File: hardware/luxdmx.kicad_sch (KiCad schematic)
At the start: 97 parts, among them J1 XLR-5 NC5FAH, J2 USB-C, J3 HY931147C, J4 DISP SH9, J5 XLR-5 NC5FAH, J6 EXP SH9, J7 DMX-OUT A, J8 DMX-OUT B, SW1 BOOT, SW2 RST, U1 ESP32-S3-WROOM-1-N8R2, U2 W5500, U4 SY8089, U5 ISO3086DWR, U6 ISO3086DWR, U7 DP9900M-5V, U8 USBLC6-2SC6, U9 TPS2116DRLR, Y1 25MHz

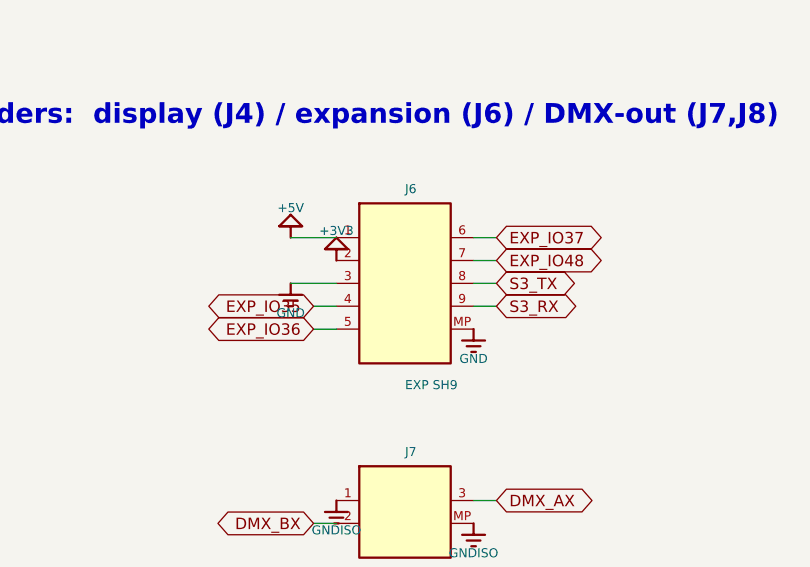
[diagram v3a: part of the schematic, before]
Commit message: hw: v6.0 -- give J4 and J6 the same power pins so a swapped cable stops killing displays
J4 (display) and J6 (expansion) are the same JST SH 9-pin part sitting 9mm apart, so a
cable happily plugs into either one. Their power pins did not agree though:

  J4:  1 = +3V3   2 = GND    3.. = signals
  J6:  1 = +5V    2 = +3V3   3   = GND   4.. = signals

so putting the display on J6 fed it +5V on VCC and +3V3 on GND. That is not a theoretical
hazard, it killed a panel on my bench. The other direction is nasty too: an expansion board
in J4 returns its whole ground current through IO4.

J6 is now 1=+3V3 2=GND 3..8=signals 9=GND, matching J4. Worst case for a mixed-up cable is
now that some 3V3 CMOS signals land in the wrong places, which both sides shrug off. A
display plugged into J6 lands RST on GND and just sits there in reset, dark but fine.

Why J6 and not J4: whichever header moves invalidates its own cables, and re-pinning J4
would have put +5V on every display cable that already exists, so the exact same dead
display with a new cause. J6's pinout only landed in v5.2 and nothing is built against it
yet, so it is the cheap one to change.

Two things fall out of that:

  * +5V is gone from J6. Feed 5V loads from your own supply.
  * pin 9 is a second GND rather than a 7th GPIO, because there is no free non-strapping
    GPIO left on the module (IO3/IO45/IO46 are all strapping pins). An extra return on a
    6-signal 1mm header is the better use anyway, and it is what makes a mis-plugged
    display land RST on ground.

New hard gate, scripts/validate_header_parity.py, wired in as gate 8. It re-checks the
invariant on the board itself every run: fatal if two different rails share a pin position
or a positive rail sits opposite a signal, GND-vs-signal allowed since that is current
limited and no worse than the GPIO-vs-GPIO contention we already accept. Ran it against the
old board first to make sure it actually catches the bug, and it fails on exactly pins 1
and 2.

Re-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
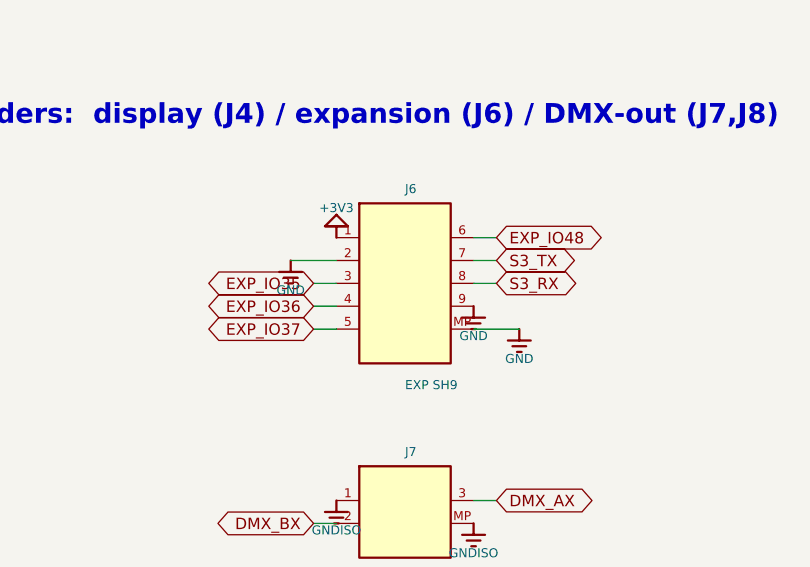
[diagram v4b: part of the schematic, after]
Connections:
- net +3V3: now also J6.1; no longer J6.2
- net +5V: no longer J6.1
- net EXP_IO35: now also J6.3; no longer J6.4
- net EXP_IO36: now also J6.4; no longer J6.5
- net EXP_IO37: now also J6.5; no longer J6.6
- net EXP_IO48: now also J6.6; no longer J6.7
- net GND: now also J6.2, J6.9; no longer J6.3
- net S3_RX: now also J6.8; no longer J6.9
- net S3_TX: now also J6.7; no longer J6.8
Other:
- title: LuxDMX v5.00 - Art-Net/sACN -> isolated DMX gateway -> LuxDMX v6.0 - Art-Net/sACN -> isolated DMX gateway
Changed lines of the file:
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@@
 	(generator_version "9.0")
 	(paper "User" 469.84 529.98)
-	(title_block (title "LuxDMX v5.00 - Art-Net/sACN -> isolated DMX gateway") (rev "v5.00") (comment 1 "auto-generated from luxdmx.net by gen_schematic.py"))
+	(title_block (title "LuxDMX v6.0 - Art-Net/sACN -> isolated DMX gateway") (rev "v6.0") (comment 1 "auto-generated from luxdmx.net by gen_schematic.py"))
 	(text "U1  ESP32-S3-WROOM-1  +  reset / boot" (exclude_from_sim no) (at 12.7 28.4 0) (effects (font (size 2.2 2.2) (bold yes)) (justify left bottom)))
 	(symbol (lib_id "luxdmx:ESP32-S3-WROOM-1-N8R2") (at 132.08 85.09 0) (unit 1) (exclude_from_sim no) (in_bom yes) (on_board yes) (dnp no)
@@
 	(wire (pts (xy 139.7 414.02) (xy 142.24 414.02)) (stroke (width 0) (type default)))
 	(global_label "DISP_RST" (shape bidirectional) (at 142.24 414.02 0) (fields_autoplaced yes) (effects (font (size 1.27 1.27)) (justify left)))
+	(wire (pts (xy 57.15 411.48) (xy 54.61 411.48)) (stroke (width 0) (type default)))
+	(global_label "EXP_IO35" (shape bidirectional) (at 54.61 411.48 0) (fields_autoplaced yes) (effects (font (size 1.27 1.27)) (justify right)))
 	(wire (pts (xy 57.15 414.02) (xy 54.61 414.02)) (stroke (width 0) (type default)))
-	(global_label "EXP_IO35" (shape bidirectional) (at 54.61 414.02 0) (fields_autoplaced yes) (effects (font (size 1.27 1.27)) (justify right)))
+	(global_label "EXP_IO36" (shape bidirectional) (at 54.61 414.02 0) (fields_autoplaced yes) (effects (font (size 1.27 1.27)) (justify right)))
 	(wire (pts (xy 57.15 416.56) (xy 54.61 416.56)) (stroke (width 0) (type default)))
-	(global_label "EXP_IO36" (shape bidirectional) (at 54.61 416.56 0) (fields_autoplaced yes) (effects (font (size 1.27 1.27)) (justify right)))
+	(global_label "EXP_IO37" (shape bidirectional) (at 54.61 416.56 0) (fields_autoplaced yes) (effects (font (size 1.27 1.27)) (justify right)))
 	(wire (pts (xy 72.39 406.4) (xy 74.93 406.4)) (stroke (width 0) (type default)))
-	(global_label "EXP_IO37" (shape bidirectional) (at 74.93 406.4 0) (fields_autoplaced yes) (effects (font (size 1.27 1.27)) (justify left)))
+	(global_label "EXP_IO48" (shape bidirectional) (at 74.93 406.4 0) (fields_autoplaced yes) (effects (font (size 1.27 1.27)) (justify left)))
 	(wire (pts (xy 72.39 408.94) (xy 74.93 408.94)) (stroke (width 0) (type default)))
-	(global_label "EXP_IO48" (shape bidirectional) (at 74.93 408.94 0) (fields_autoplaced yes) (effects (font (size 1.27 1.27)) (justify left)))
+	(global_label "S3_TX" (shape bidirectional) (at 74.93 408.94 0) (fields_autoplaced yes) (effects (font (size 1.27 1.27)) (justify left)))
 	(wire (pts (xy 72.39 411.48) (xy 74.93 411.48)) (stroke (width 0) (type default)))
-	(global_label "S3_TX" (shape bidirectional) (at 74.93 411.48 0) (fields_autoplaced yes) (effects (font (size 1.27 1.27)) (justify left)))
-	(wire (pts (xy 72.39 414.02) (xy 74.93 414.02)) (stroke (width 0) (type default)))
-	(global_label "S3_RX" (shape bidirectional) (at 74.93 414.02 0) (fields_autoplaced yes) (effects (font (size 1.27 1.27)) (justify left)))
+	(global_label "S3_RX" (shape bidirectional) (at 74.93 411.48 0) (fields_autoplaced yes) (effects (font (size 1.27 1.27)) (justify left)))
 	(wire (pts (xy 57.15 438.15) (xy 54.61 438.15)) (stroke (width 0) (type default)))
 	(global_label "DMX_BX" (shape bidirectional) (at 54.61 438.15 0) (fields_autoplaced yes) (effects (font (size 1.27 1.27)) (justify right)))
@@
 		(instances (project "luxdmx" (path "/052ade30-43eb-58ee-83e7-8a1cc2fa5955" (reference "#PWR_d7f59803-5728-5bef-b4db-1aabe809047e") (unit 1))))
 	)
-	(symbol (lib_id "luxdmx:PWR0") (at 57.15 408.94 0) (unit 1) (exclude_from_sim no) (in_bom yes) (on_board yes) (dnp no)
-		(property "Reference" "#PWR_+3V3" (at 57.15 408.94 0) (effects (font (size 1.27 1.27)) (hide yes)))
-		(property "Value" "+3V3" (at 57.15 405.64 0) (effects (font (size 1 1))))
-		(instances (project "luxdmx" (path "/052ade30-43eb-58ee-83e7-8a1cc2fa5955" (reference "#PWR_3f9a2aac-3b20-520b-8f6c-e2b5555b1456") (unit 1))))
+	(symbol (lib_id "luxdmx:PWR0") (at 57.15 406.4 0) (unit 1) (exclude_from_sim no) (in_bom yes) (on_board yes) (dnp no)
+		(property "Reference" "#PWR_+3V3" (at 57.15 406.4 0) (effects (font (size 1.27 1.27)) (hide yes)))
+		(property "Value" "+3V3" (at 57.15 403.1 0) (effects (font (size 1 1))))
+		(instances (project "luxdmx" (path "/052ade30-43eb-58ee-83e7-8a1cc2fa5955" (reference "#PWR_d79cf4fe-2cfb-5adf-90e1-6d4bfc1883d8") (unit 1))))
 	)
 	(wire (pts (xy 124.46 408.94) (xy 119.38 408.94)) (stroke (width 0) (type default)))
@@
 		(instances (project "luxdmx" (path "/052ade30-43eb-58ee-83e7-8a1cc2fa5955" (reference "#PWR_56f6acff-e593-5096-b85d-3b8d9c72a26a") (unit 1))))
 	)
-	(wire (pts (xy 57.15 411.48) (xy 52.07 411.48)) (stroke (width 0) (type default)))
-	(symbol (lib_id "luxdmx:PWR6") (at 52.07 411.48 0) (unit 1) (exclude_from_sim no) (in_bom yes) (on_board yes) (dnp no)
-		(property "Reference" "#PWR_GND" (at 52.07 411.48 0) (effects (font (size 1.27 1.27)) (hide yes)))
-		(property "Value" "GND" (at 52.07 414.78 0) (effects (font (size 1 1))))
-		(instances (project "luxdmx" (path "/052ade30-43eb-58ee-83e7-8a1cc2fa5955" (reference "#PWR_0554def3-d116-52d7-9d76-2ec781469eac") (unit 1))))
-	)
-	(symbol (lib_id "luxdmx:PWR6") (at 72.39 416.56 0) (unit 1) (exclude_from_sim no) (in_bom yes) (on_board yes) (dnp no)
-		(property "Reference" "#PWR_GND" (at 72.39 416.56 0) (effects (font (size 1.27 1.27)) (hide yes)))
-		(property "Value" "GND" (at 72.39 419.86 0) (effects (font (size 1 1))))
-		(instances (project "luxdmx" (path "/052ade30-43eb-58ee-83e7-8a1cc2fa5955" (reference "#PWR_87fad163-71c5-5b82-8a55-77bac8619c2b") (unit 1))))
-	)
-	(wire (pts (xy 57.15 406.4) (xy 52.07 406.4)) (stroke (width 0) (type default)))
-	(symbol (lib_id "luxdmx:PWR1") (at 52.07 406.4 0) (unit 1) (exclude_from_sim no) (in_bom yes) (on_board yes) (dnp no)
-		(property "Reference" "#PWR_+5V" (at 52.07 406.4 0) (effects (font (size 1.27 1.27)) (hide yes)))
-		(property "Value" "+5V" (at 52.07 403.1 0) (effects (font (size 1 1))))
-		(instances (project "luxdmx" (path "/052ade30-43eb-58ee-83e7-8a1cc2fa5955" (reference "#PWR_3a30b7fb-2b1b-5178-8cd5-bc8e4585f861") (unit 1))))
+	(wire (pts (xy 57.15 408.94) (xy 52.07 408.94)) (stroke (width 0) (type default)))
+	(symbol (lib_id "luxdmx:PWR6") (at 52.07 408.94 0) (unit 1) (exclude_from_sim no) (in_bom yes) (on_board yes) (dnp no)
+		(property "Reference" "#PWR_GND" (at 52.07 408.94 0) (effects (font (size 1.27 1.27)) (hide yes)))
+		(property "Value" "GND" (at 52.07 412.24 0) (effects (font (size 1 1))))
+		(instances (project "luxdmx" (path "/052ade30-43eb-58ee-83e7-8a1cc2fa5955" (reference "#PWR_90228f89-7916-58df-89f3-f8f4c3c5f623") (unit 1))))
+	)
+	(symbol (lib_id "luxdmx:PWR6") (at 72.39 414.02 0) (unit 1) (exclude_from_sim no) (in_bom yes) (on_board yes) (dnp no)
+		(property "Reference" "#PWR_GND" (at 72.39 414.02 0) (effects (font (size 1.27 1.27)) (hide yes)))
+		(property "Value" "GND" (at 72.39 417.32 0) (effects (font (size 1 1))))
+		(instances (project "luxdmx" (path "/052ade30-43eb-58ee-83e7-8a1cc2fa5955" (reference "#PWR_db845f92-c338-5a90-8362-3d3019c163bd") (unit 1))))
+	)
+	(wire (pts (xy 72.39 416.56) (xy 77.47 416.56)) (stroke (width 0) (type default)))
+	(symbol (lib_id "luxdmx:PWR6") (at 77.47 416.56 0) (unit 1) (exclude_from_sim no) (in_bom yes) (on_board yes) (dnp no)
+		(property "Reference" "#PWR_GND" (at 77.47 416.56 0) (effects (font (size 1.27 1.27)) (hide yes)))
+		(property "Value" "GND" (at 77.47 419.86 0) (effects (font (size 1 1))))
+		(instances (project "luxdmx" (path "/052ade30-43eb-58ee-83e7-8a1cc2fa5955" (reference "#PWR_1d16cae9-f614-5966-a9d6-7de75373a57a") (unit 1))))
 	)
 	(symbol (lib_id "luxdmx:PWR7") (at 57.15 435.61 0) (unit 1) (exclude_from_sim no) (in_bom yes) (on_board yes) (dnp no)
